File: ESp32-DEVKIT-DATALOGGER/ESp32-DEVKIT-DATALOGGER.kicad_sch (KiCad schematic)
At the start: 9 parts, among them J1 Socket_01x02, J2 Conn_01x04, SW1 SW_Omron_B3FS, U1 ESP32-S3-MINI-1-N8

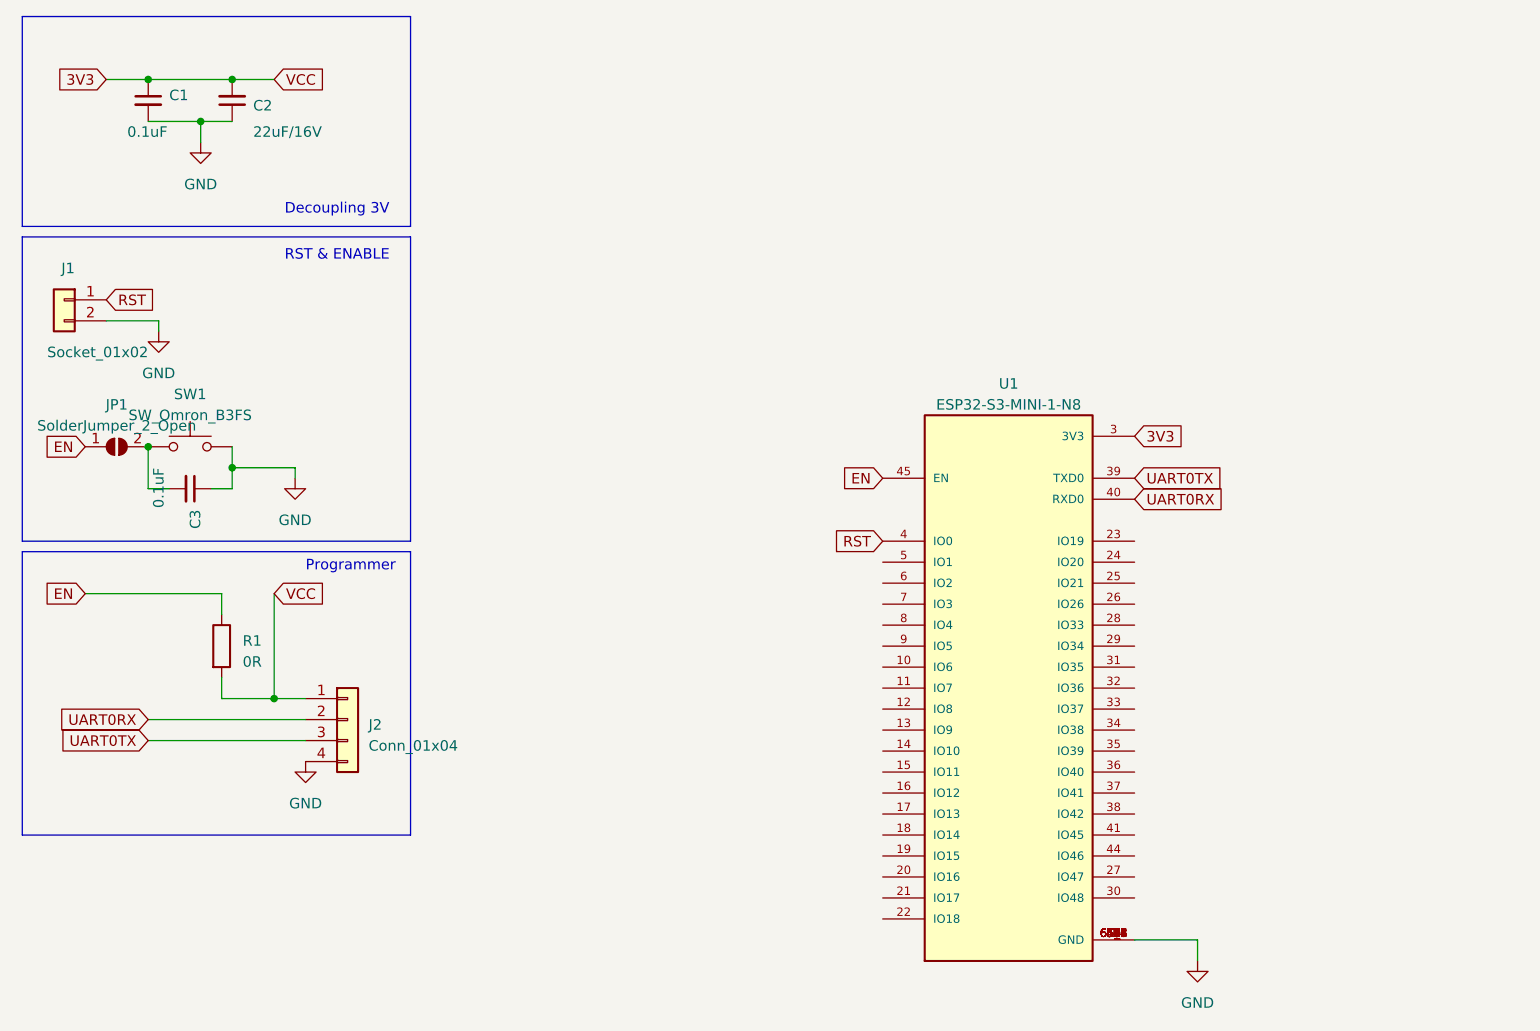
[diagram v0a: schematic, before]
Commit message: Basic Structure made, need more refining and parts
Add the Filtering to the CAN and RS485, If make money this month
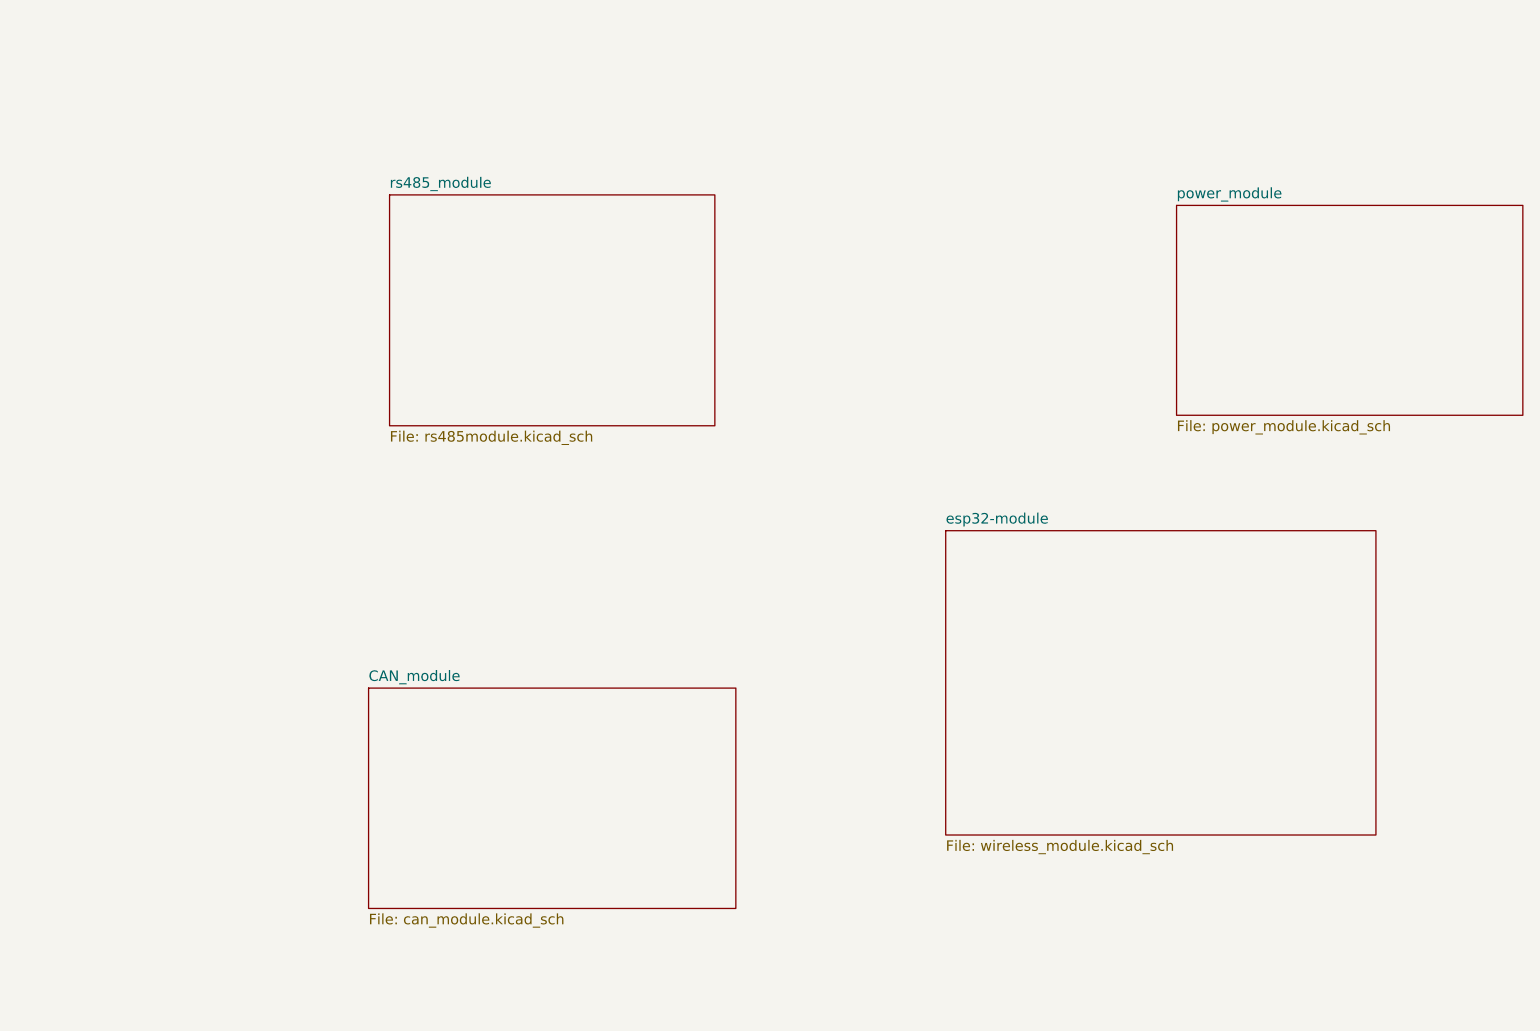
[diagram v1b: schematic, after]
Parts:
- removed C1, C3: 0.1uF_0603_16V, PCM_Capacitor_SMD_AKL:C_0603_1608Metric_Pad1.08x0.95mm, symbol PCM_4ms_Capacitor:0.1uF_0603_16V
- removed C2: 22uF_0603_16V, PCM_Capacitor_SMD_AKL:C_0603_1608Metric_Pad1.08x0.95mm, symbol PCM_4ms_Capacitor:22uF_0603_16V
- removed J1: Socket_01x02, PCM_Jumper_AKL:Jumper_P2.54mm_D0.7mm, symbol PCM_4ms_Connector:Socket_01x02
- removed J2: Conn_01x04, Connector_PinHeader_2.54mm:PinHeader_1x04_P2.54mm_Vertical, symbol PCM_4ms_Connector:Conn_01x04
- removed JP1: SolderJumper_2_Open, Jumper:SolderJumper-2_P1.3mm_Open_TrianglePad1.0x1.5mm, symbol Jumper:SolderJumper_2_Open
- removed R1: 0R_0603, PCM_4ms_Resistor:R_0603, symbol PCM_4ms_Resistor:0R_0603
- removed SW1: SW_Omron_B3FS, Button_Switch_SMD:SW_Tactile_SPST_NO_Straight_CK_PTS636Sx25SMTRLFS, symbol Switch:SW_Omron_B3FS
- removed U1: ESP32-S3-MINI-1-N8, XCVR_ESP32-S3-MINI-1-N8, symbol ESP32-S3-MINI-1-N8:ESP32-S3-MINI-1-N8
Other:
- added sheet CAN_module (can_module.kicad_sch)
- added sheet esp32-module (wireless_module.kicad_sch)
- added sheet power_module (power_module.kicad_sch)
- added sheet rs485_module (rs485module.kicad_sch)
- note removed: "Decoupling 3V"
- note removed: "Programmer"
- note removed: "RST & ENABLE"
